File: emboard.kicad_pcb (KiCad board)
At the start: 2 copper layers, 85.6 x 54 mm, 2 parts

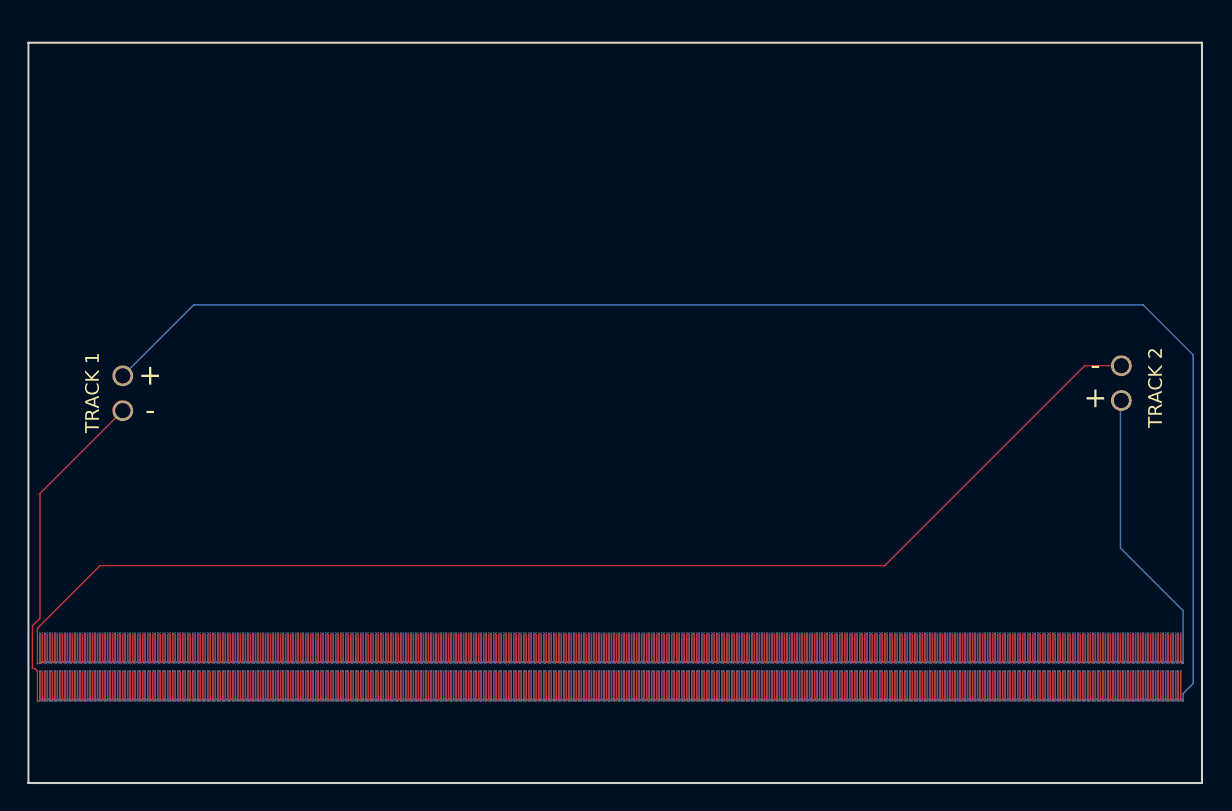
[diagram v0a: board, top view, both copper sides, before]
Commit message: more affordable tolerances
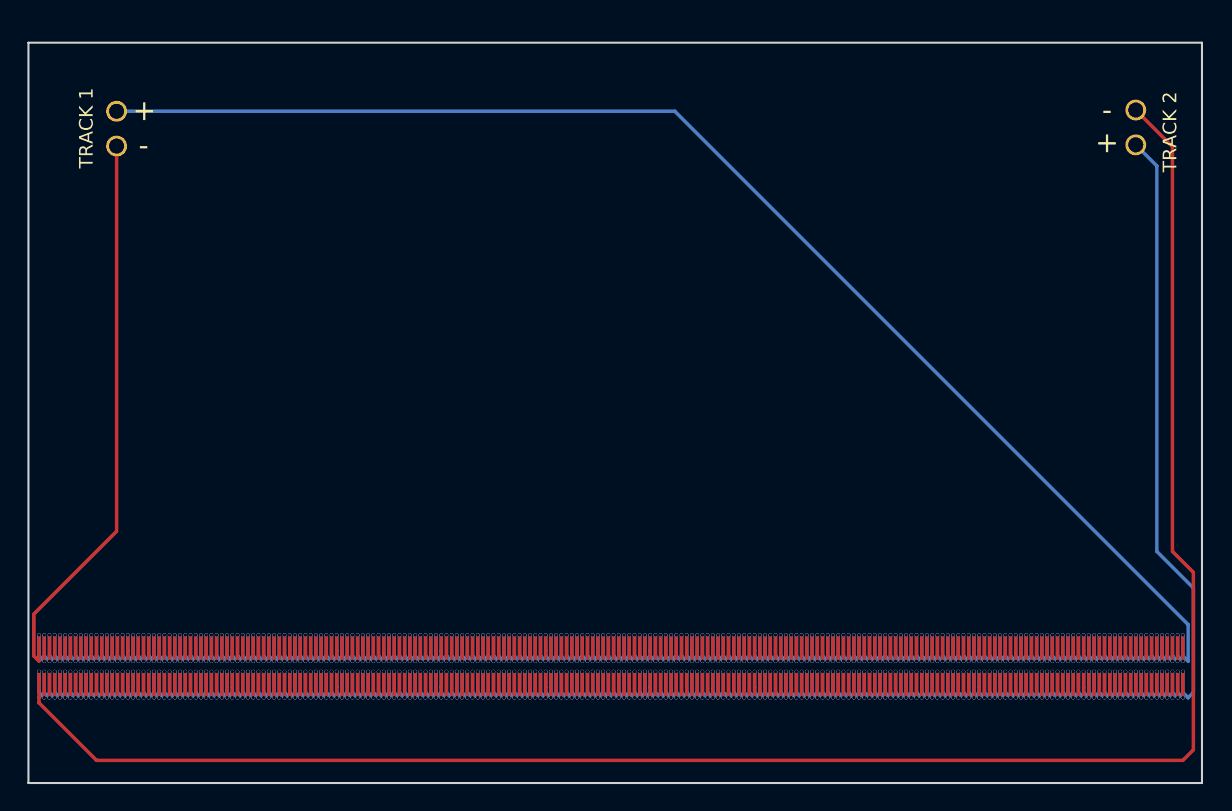
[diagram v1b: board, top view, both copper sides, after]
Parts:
- moved TRACK 1 19.3 mm to (81.3, 70.0)
- moved TRACK 2 18.7 mm to (165.8, 72.5)
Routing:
- net (no net): track 0.00 -> 2059.7 mm, vias 0 -> 878
- net +1: track 1121.1 -> 0.00 mm, vias 454 -> 0
- net -2: track 1078.7 -> 0.00 mm, vias 442 -> 0
- net +2: track 1068.1 -> 0.09 mm, vias 470 -> 1
- net -1: track 1046.6 -> 0.00 mm, vias 457 -> 0
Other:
- net class Default: clearance 0.0762 -> 0.127
- rule trace_clearance: 0.0762 -> 0.127
- rule via_min_drill: 0.1 -> 0.254
- rule via_min_size: 0.1 -> 0.255

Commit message: better tolerances
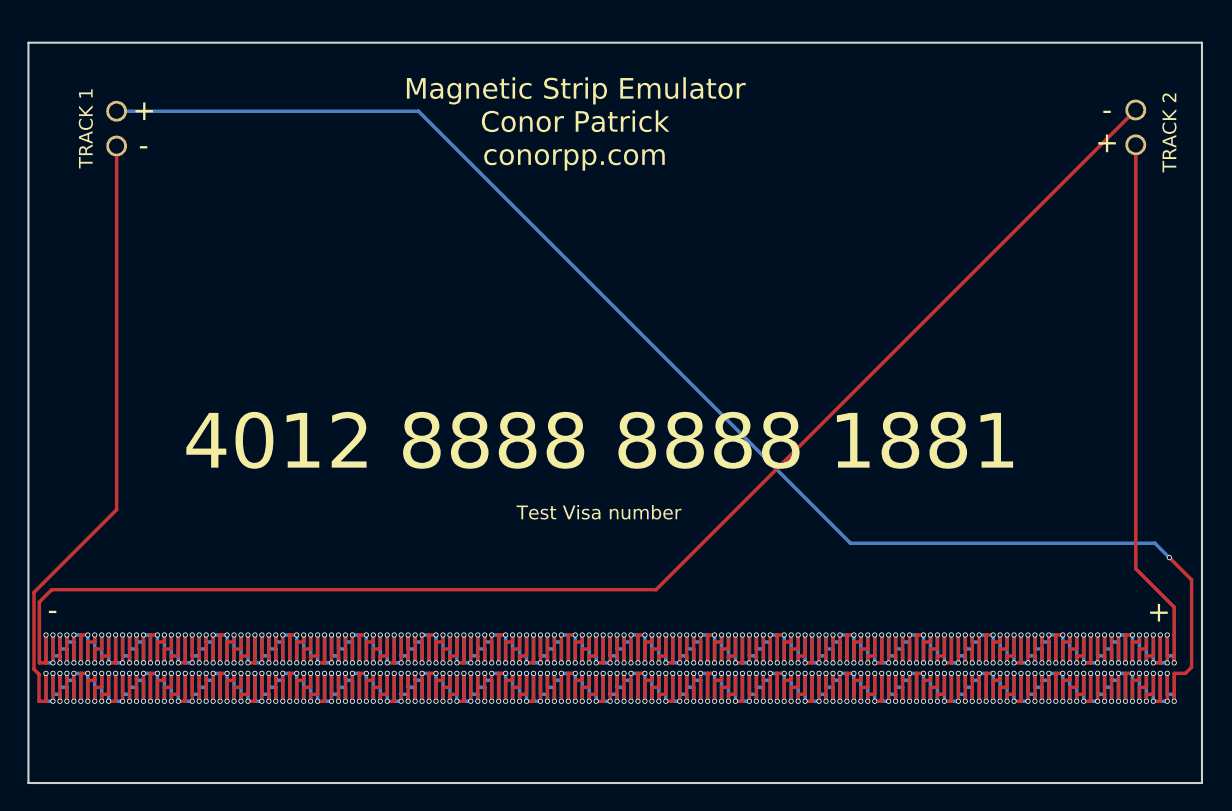
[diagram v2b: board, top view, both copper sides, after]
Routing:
- net (no net): track 2059.7 -> 0.00 mm, vias 878 -> 0
- net +1: track 0.00 -> 442.8 mm, vias 0 -> 149
- net -2: track 0.00 -> 437.1 mm, vias 0 -> 145
- net -1: track 0.00 -> 378.9 mm, vias 0 -> 144
- net +2: track 0.09 -> 377.4 mm, vias 1 -> 148
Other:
- board text added: "4012 8888 8888 1881"
- board text added: "Magnetic Strip Emulator Conor Patrick conorpp.com"
- board text added: "Test Visa number"

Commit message: add buttons
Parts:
- added Button Left: 2pin-header, footprints:2pin-header, F.Cu at (99.0, 62.1)
- added Button Right: 2pin-header, footprints:2pin-header, F.Cu at (148.0, 62.2)
- moved TRACK 1 1.03 mm to (81.5, 69.0)
- moved TRACK 2 1.03 mm to (166.0, 71.4)
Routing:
- net (no net): track 0.00 -> 284.5 mm, vias 0 -> 5
- net -1: track 378.9 -> 358.1 mm, vias 144 -> 136
- net +1: track 442.8 -> 463.5 mm, vias 149 -> 157

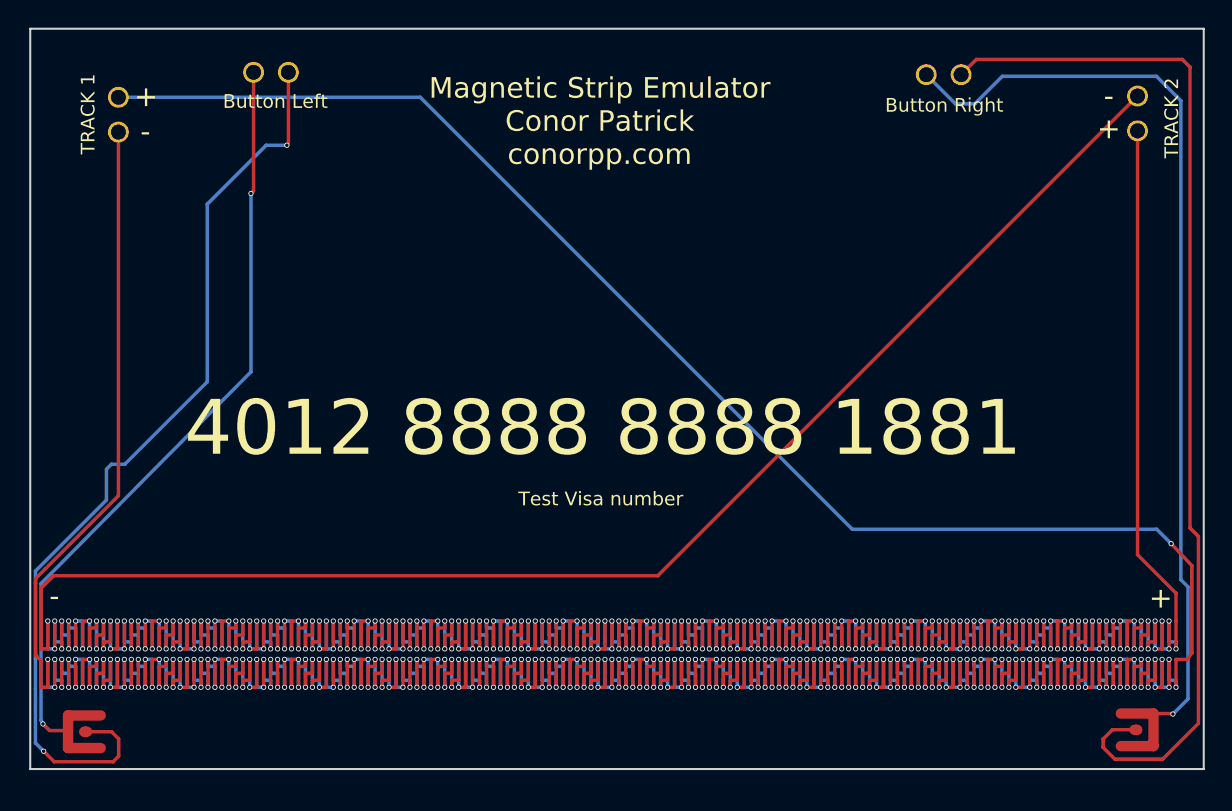
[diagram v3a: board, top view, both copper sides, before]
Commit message: change snaptron button and make coil uniform
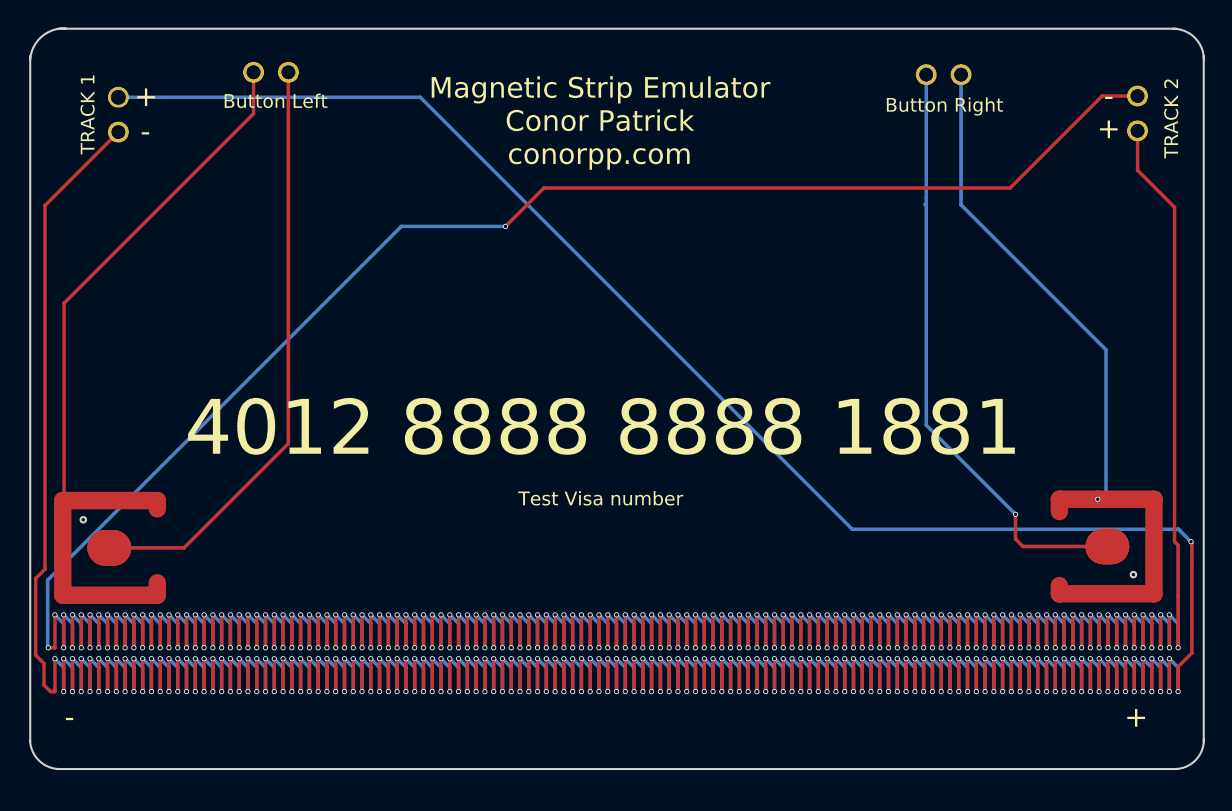
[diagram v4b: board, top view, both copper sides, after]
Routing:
- net (no net): track 284.5 -> 0.00 mm, vias 5 -> 0
- net Buttonleft2: track 0.00 -> 59.2 mm
- net buttonright1: track 0.00 -> 57.8 mm, vias 0 -> 1
- net +1: track 463.5 -> 414.9 mm, vias 157 -> 125
- net Buttonleft1: track 0.00 -> 44.8 mm
- net buttonright2: track 0.00 -> 44.6 mm, vias 0 -> 1
- net -2: track 437.1 -> 408.6 mm, vias 145 -> 124
- net -1: track 358.1 -> 380.9 mm, vias 136 -> 132
- net +2: track 377.4 -> 378.4 mm, vias 148 -> 135
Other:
- outline, holes or cut-outs redrawn

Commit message: make long ways
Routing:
- net (no net): track 0.00 -> 1328.9 mm, vias 0 -> 16
- net -1: track 380.9 -> 1167.9 mm, vias 132 -> 14
- net -2: track 408.6 -> 0.00 mm, vias 124 -> 0
- net +2: track 378.4 -> 0.09 mm, vias 135 -> 1
- net +1: track 414.9 -> 46.2 mm, vias 125 -> 0
- net Buttonleft1: track 44.8 -> 44.0 mm
- net Buttonleft2: track 59.2 -> 59.7 mm, vias 0 -> 1
- net buttonright2: track 44.6 -> 45.1 mm, vias 1 -> 0
- net buttonright1: track 57.8 -> 57.9 mm, vias 1 -> 0
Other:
- outline, holes or cut-outs redrawn
